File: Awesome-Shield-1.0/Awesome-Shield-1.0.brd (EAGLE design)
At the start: 51 x 55 mm, 21 parts, among them J1 PORT1, J2 PORT2, J3 PORT3, SW1 SPST_TACT-EVQQ2, SW2 DPDT, U1 LIGHTSENSORTEMT6000, X1 PASSER-07, X2 PASSER-07

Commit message: nudged resistor
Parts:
- moved R2 0.63 mm to (12.7, 45.7)
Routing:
- net N$3: track 10.2 -> 11.2 mm
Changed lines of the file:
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@@
 <element name="R1" library="rcl" package="R1206" value="TBD" x="31.115" y="46.99" smashed="yes" rot="R180"/>
 <element name="U$1" library="buzzer-loudity-bzel-t68-0808" package="SMT-68" value="LOUDITY-BZEL-T680808" x="38.735" y="43.18" smashed="yes" rot="R90"/>
-<element name="R2" library="we-rcl" package="C1206" value="330R" x="12.065" y="45.72"/>
+<element name="R2" library="we-rcl" package="C1206" value="330R" x="12.7" y="45.72"/>
 <element name="X1" library="we-symbol" package="PASSER_07MM" value="PASSER-07" x="1.27" y="48.26"/>
 <element name="X2" library="we-symbol" package="PASSER_07MM" value="PASSER-07" x="47.625" y="5.08"/>
@@
 <contactref element="R2" pad="1"/>
 <wire x1="13.335" y1="48.26" x2="12.195" y2="47.12" width="0.254" layer="1"/>
-<wire x1="12.195" y1="47.12" x2="12.065" y2="47.12" width="0.254" layer="1"/>
+<wire x1="12.195" y1="47.12" x2="12.7" y2="47.12" width="0.254" layer="1"/>
 <wire x1="13.335" y1="48.26" x2="14.605" y2="48.26" width="0.254" layer="1"/>
 <wire x1="14.605" y1="48.26" x2="15.24" y2="47.625" width="0.254" layer="1"/>
@@
 <wire x1="11.43" y1="39.37" x2="11.43" y2="40.64" width="0.254" layer="1"/>
 <wire x1="11.43" y1="40.64" x2="10.16" y2="41.91" width="0.254" layer="1"/>
-<wire x1="10.16" y1="41.91" x2="10.16" y2="48.26" width="0.254" layer="1"/>
-<wire x1="10.16" y1="48.26" x2="10.795" y2="48.895" width="0.254" layer="1"/>
-<wire x1="10.795" y1="48.895" x2="22.987" y2="48.895" width="0.254" layer="1"/>
-<wire x1="22.987" y1="48.895" x2="24.892" y2="46.99" width="0.254" layer="1"/>
+<wire x1="23.241" y1="48.641" x2="24.892" y2="46.99" width="0.254" layer="1"/>
 <wire x1="24.892" y1="46.99" x2="26.67" y2="46.99" width="0.254" layer="1"/>
 <via x="26.67" y="46.99" extent="1-16" drill="0.7" diameter="1.27"/>
 <wire x1="26.67" y1="46.99" x2="35.56" y2="46.99" width="0.254" layer="16"/>
 <wire x1="35.56" y1="46.99" x2="39.37" y2="50.8" width="0.254" layer="16"/>
+<wire x1="10.16" y1="41.91" x2="10.16" y2="44.45" width="0.254" layer="1"/>
+<wire x1="10.16" y1="44.45" x2="10.795" y2="45.085" width="0.254" layer="1"/>
+<wire x1="10.795" y1="45.085" x2="10.795" y2="48.26" width="0.254" layer="1"/>
+<wire x1="10.795" y1="48.26" x2="11.43" y2="48.895" width="0.254" layer="1"/>
+<wire x1="11.43" y1="48.895" x2="22.987" y2="48.895" width="0.254" layer="1"/>
+<wire x1="22.987" y1="48.895" x2="23.241" y2="48.641" width="0.254" layer="1"/>
 </signal>
 <signal name="A3">
@@
 <contactref element="R2" pad="2"/>
 <contactref element="D1" pad="4"/>
-<wire x1="12.065" y1="44.32" x2="10.795" y2="43.05" width="0.254" layer="1"/>
-<wire x1="10.795" y1="43.05" x2="10.795" y2="42.545" width="0.254" layer="1"/>
 <wire x1="10.795" y1="42.545" x2="12.7" y2="40.64" width="0.254" layer="1"/>
 <wire x1="12.7" y1="40.64" x2="17.438" y2="40.64" width="0.254" layer="1"/>
 <wire x1="17.438" y1="40.64" x2="17.743" y2="40.945" width="0.254" layer="1"/>
+<wire x1="12.7" y1="44.32" x2="11.3" y2="44.32" width="0.254" layer="1"/>
+<wire x1="11.3" y1="44.32" x2="10.795" y2="43.815" width="0.254" layer="1"/>
+<wire x1="10.795" y1="43.815" x2="10.795" y2="42.545" width="0.254" layer="1"/>
 </signal>
 </signals>

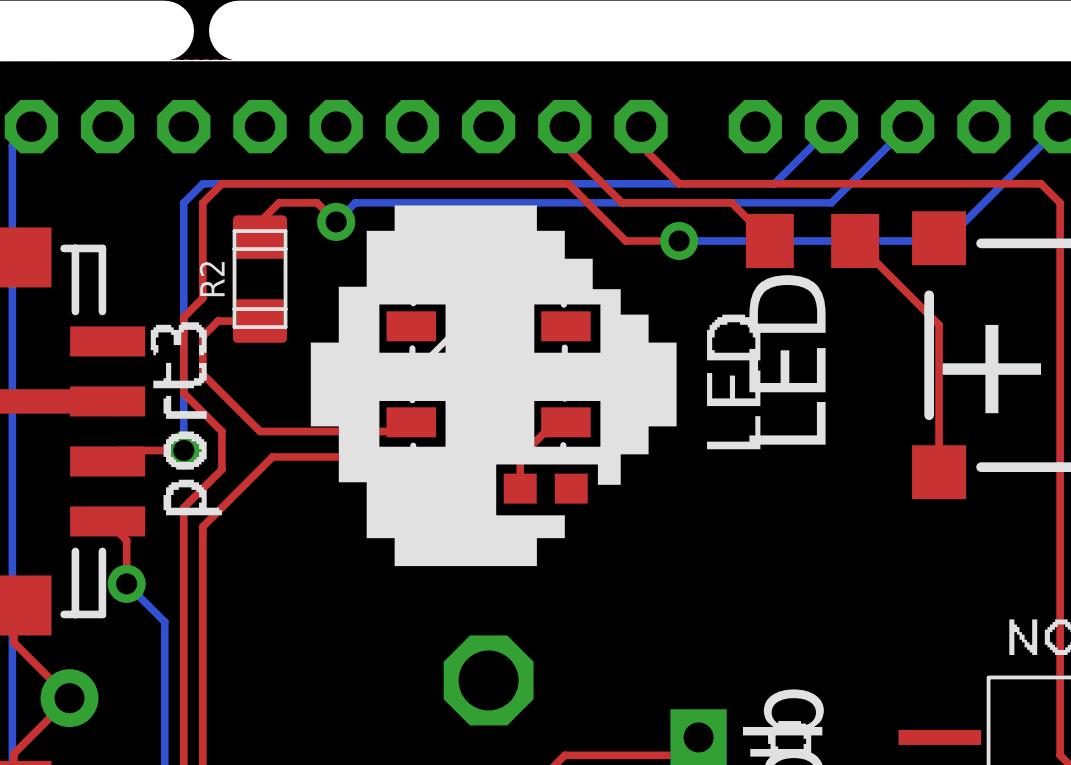
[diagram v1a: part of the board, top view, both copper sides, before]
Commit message: nudged LED C and R for component spacing :shipit:
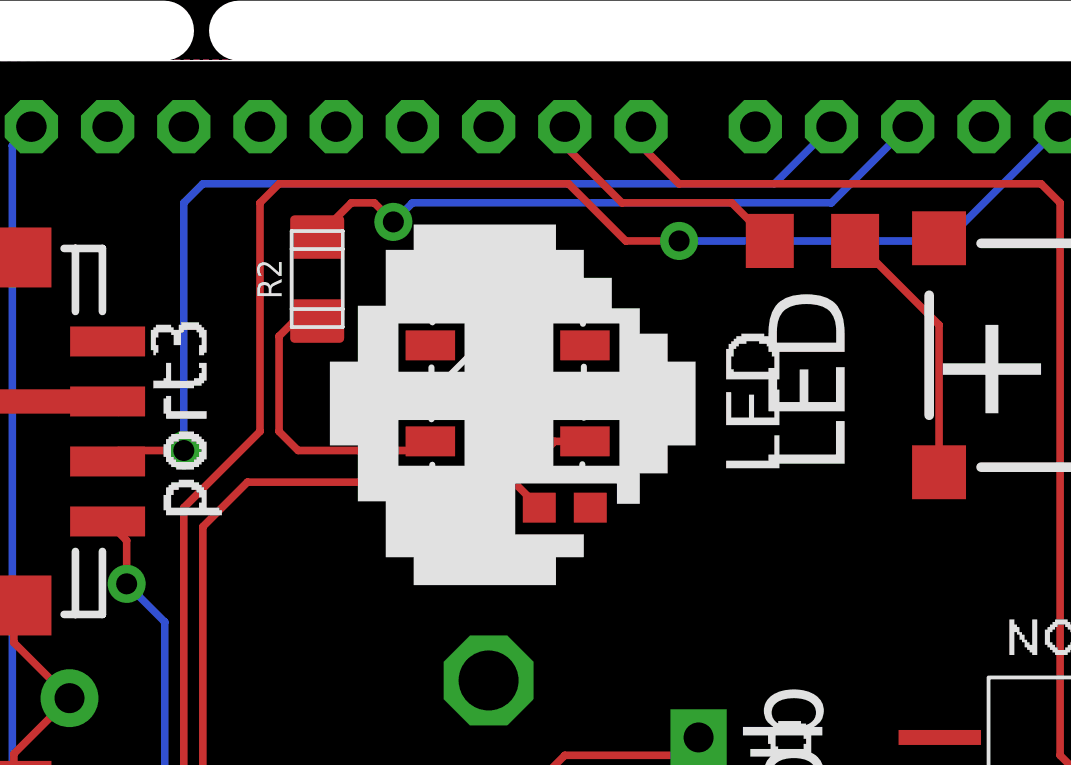
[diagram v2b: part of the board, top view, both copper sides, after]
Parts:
- moved R2 1.91 mm to (14.6, 45.7)
- moved D1 0.90 mm to (21.0, 41.9)
- moved C1 0.90 mm to (22.9, 38.1)
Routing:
- net D5: track 24.7 -> 21.7 mm
- net D3: track 60.9 -> 58.7 mm
- net N$3: track 11.2 -> 10.1 mm
